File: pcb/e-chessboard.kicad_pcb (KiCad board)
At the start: 4 copper layers, 170 x 170 mm, 66 parts, among them J1 POWER, J2 UART, Q1 BC847, Q2 BC847, SW1 Reset, SW2 Boot, U1 ESP32-WROOM-32U, U10 MAGNET_LDR, U11 MAGNET_LDR, U12 MAGNET_LDR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

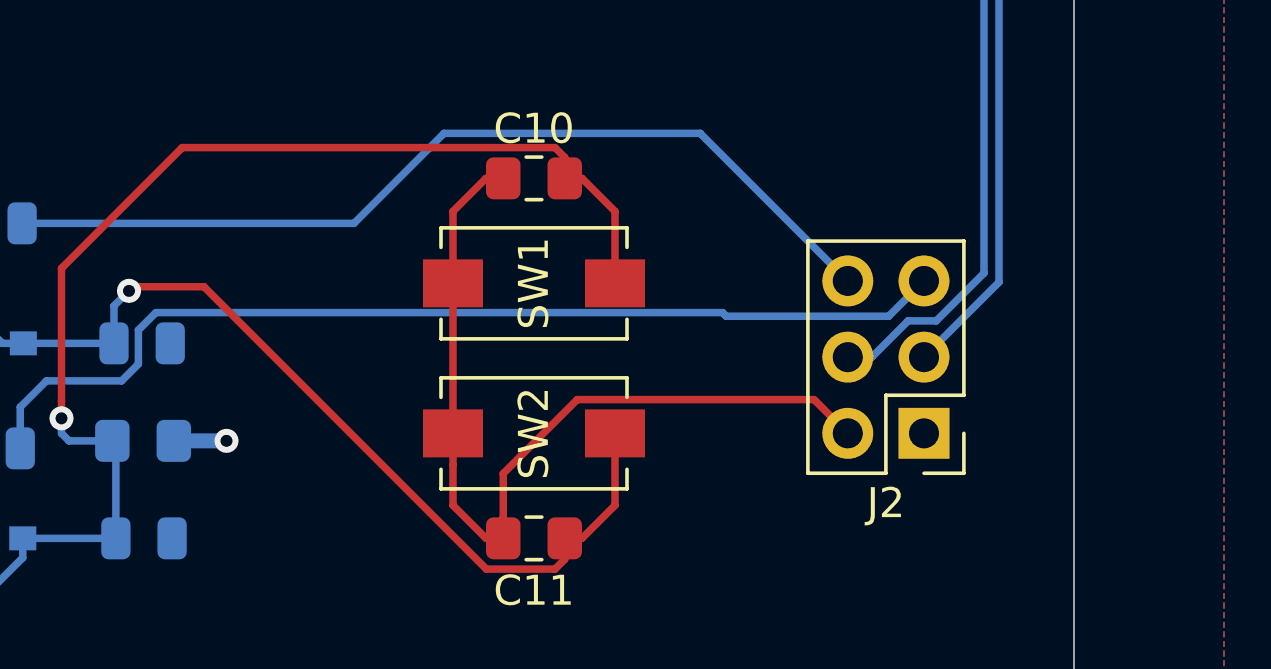
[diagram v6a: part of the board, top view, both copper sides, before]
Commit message: fix(kicad): adding label for taster and uart
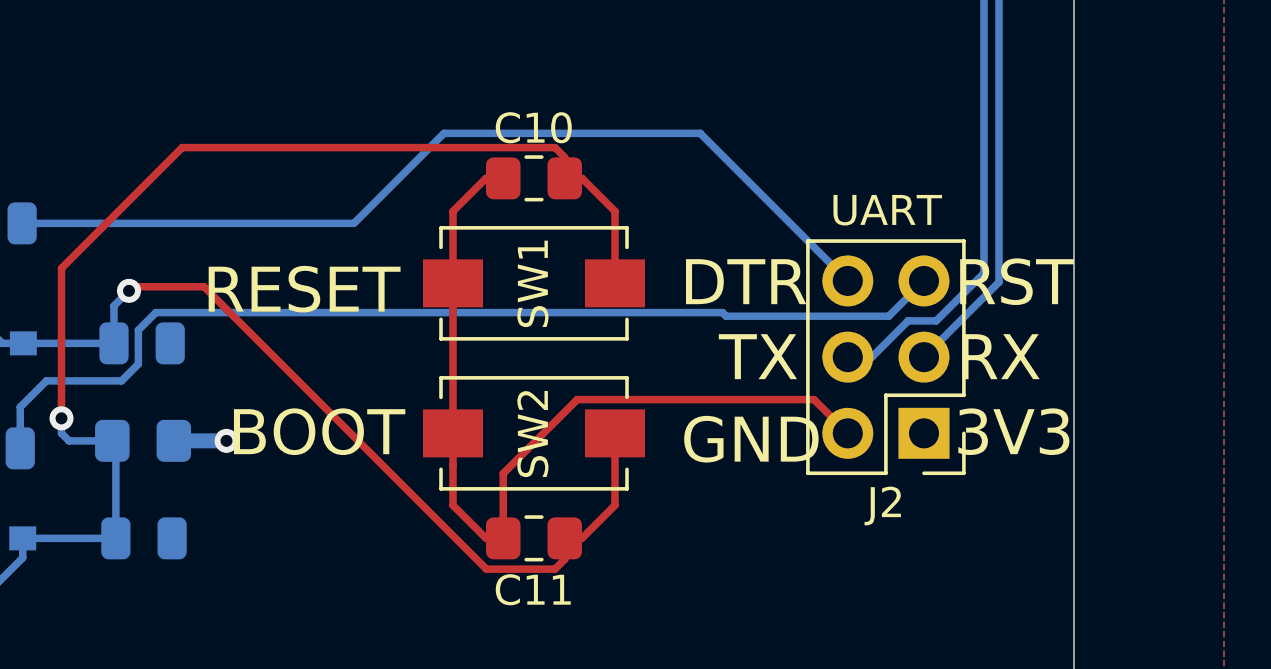
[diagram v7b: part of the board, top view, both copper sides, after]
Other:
- board text added: "3V3"
- board text added: "BOOT"
- board text added: "DTR"
- board text added: "GND"
- board text added: "RESET"
- board text added: "RST"
- board text added: "RX"
- board text added: "TX"
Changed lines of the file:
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@@
   (general
     (thickness 1.6)
-    (drawings 22)
+    (drawings 30)
     (tracks 537)
     (zones 0)
@@
       (effects (font (size 1 1) (thickness 0.15)))
     )
-    (fp_text value UART (at 1.27 7.41 180) (layer F.Fab)
+    (fp_text value UART (at 1.27 7.41 180) (layer F.SilkS)
       (effects (font (size 1 1) (thickness 0.15)))
     )
@@
     )
   )
+  (gr_text BOOT (at 194.75 112) (layer F.SilkS)
+    (effects (font (size 1.5 1.5) (thickness 0.3)))
+  )
+  (gr_text RESET (at 194.25 107.25) (layer F.SilkS)
+    (effects (font (size 1.5 1.5) (thickness 0.3)))
+  )
+  (gr_text DTR (at 209 107) (layer F.SilkS)
+    (effects (font (size 1.5 1.5) (thickness 0.3)))
+  )
+  (gr_text TX (at 209.5 109.5) (layer F.SilkS)
+    (effects (font (size 1.5 1.5) (thickness 0.3)))
+  )
+  (gr_text GND (at 209.25 112.25) (layer F.SilkS)
+    (effects (font (size 1.5 1.5) (thickness 0.3)))
+  )
+  (gr_text 3V3 (at 218 112) (layer F.SilkS)
+    (effects (font (size 1.5 1.5) (thickness 0.3)))
+  )
+  (gr_text RX (at 217.5 109.5) (layer F.SilkS)
+    (effects (font (size 1.5 1.5) (thickness 0.3)))
+  )
+  (gr_text RST (at 218 107) (layer F.SilkS)
+    (effects (font (size 1.5 1.5) (thickness 0.3)))
+  )
   (gr_line (start 220 55) (end 220 85) (layer Edge.Cuts) (width 0.05))
   (gr_line (start 220 215) (end 220 85) (layer Edge.Cuts) (width 0.05))
@@
     (connect_pads (clearance 0.508))
     (min_thickness 0.254)
-    (fill yes (arc_segments 32) (thermal_gap 0.508) (thermal_bridge_width 0.508))
+    (fill (arc_segments 32) (thermal_gap 0.508) (thermal_bridge_width 0.508))
     (polygon
       (pts
@@
     (connect_pads (clearance 0.508))
     (min_thickness 0.254)
-    (fill yes (arc_segments 32) (thermal_gap 0.508) (thermal_bridge_width 0.508))
+    (fill (arc_segments 32) (thermal_gap 0.508) (thermal_bridge_width 0.508))
     (polygon
       (pts
@@
     (connect_pads (clearance 0.508))
     (min_thickness 0.254)
-    (fill yes (arc_segments 32) (thermal_gap 0.508) (thermal_bridge_width 0.508))
+    (fill (arc_segments 32) (thermal_gap 0.508) (thermal_bridge_width 0.508))
     (polygon
       (pts
@@
     (connect_pads (clearance 0.508))
     (min_thickness 0.254)
-    (fill yes (arc_segments 32) (thermal_gap 0.508) (thermal_bridge_width 0.508))
+    (fill (arc_segments 32) (thermal_gap 0.508) (thermal_bridge_width 0.508))
     (polygon
       (pts

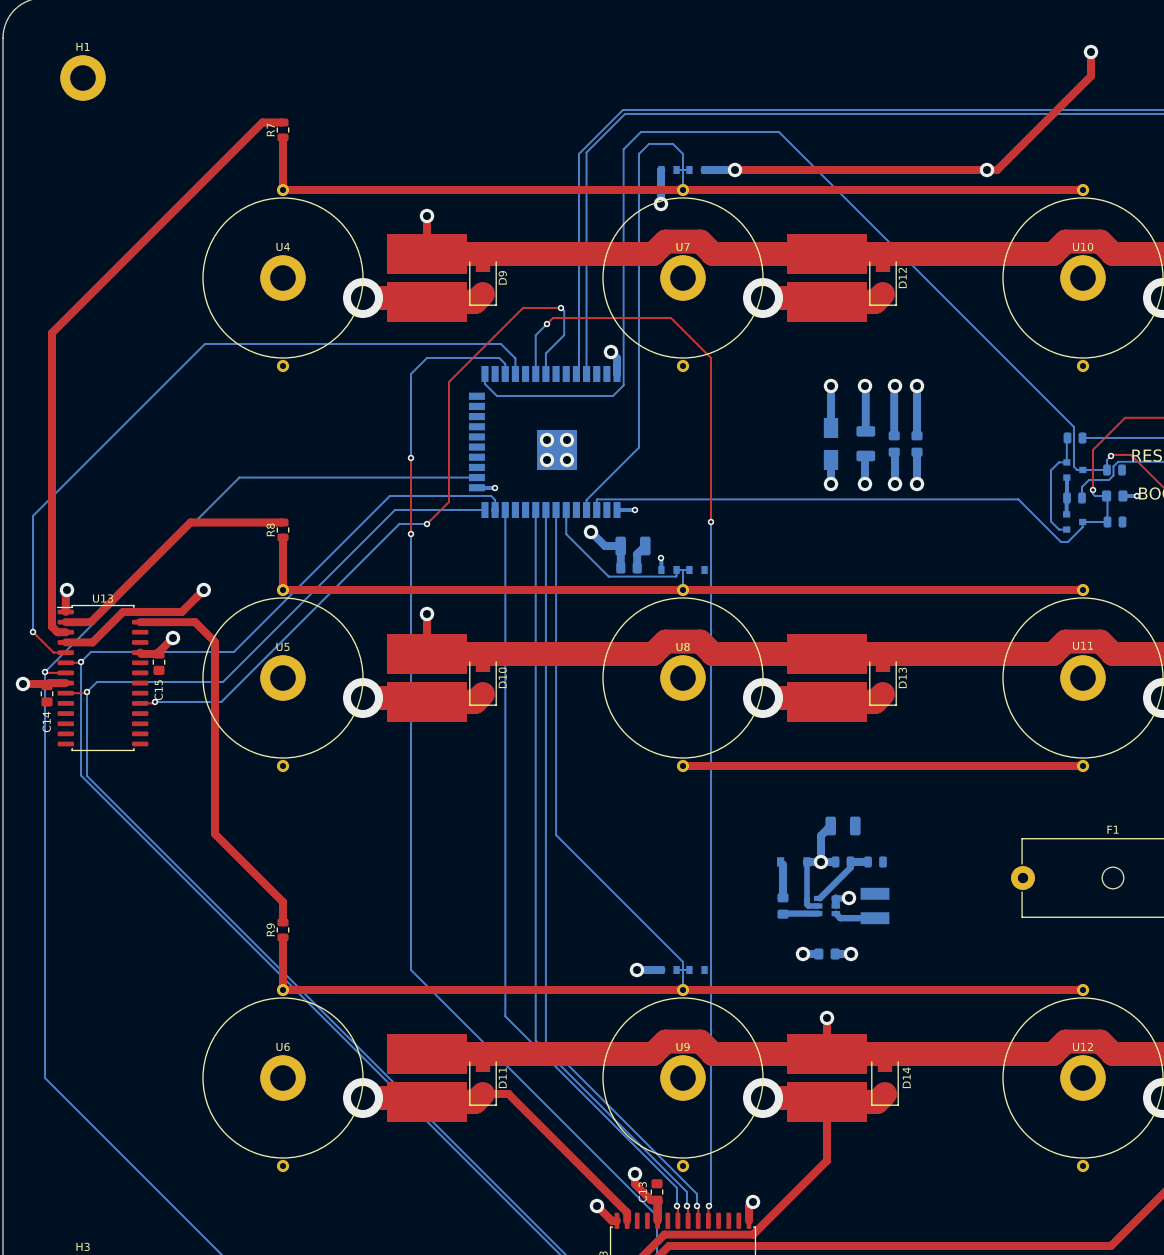
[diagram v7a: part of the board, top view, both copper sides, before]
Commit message: fix(kicad): redesign pcb
Redesigning the pcb with the new ldr matrix.
I'm pretty sure, that's it's still not working, but for the first
prototype I will put the focus on the magnets and not the ldr. Just a
prove a concept.
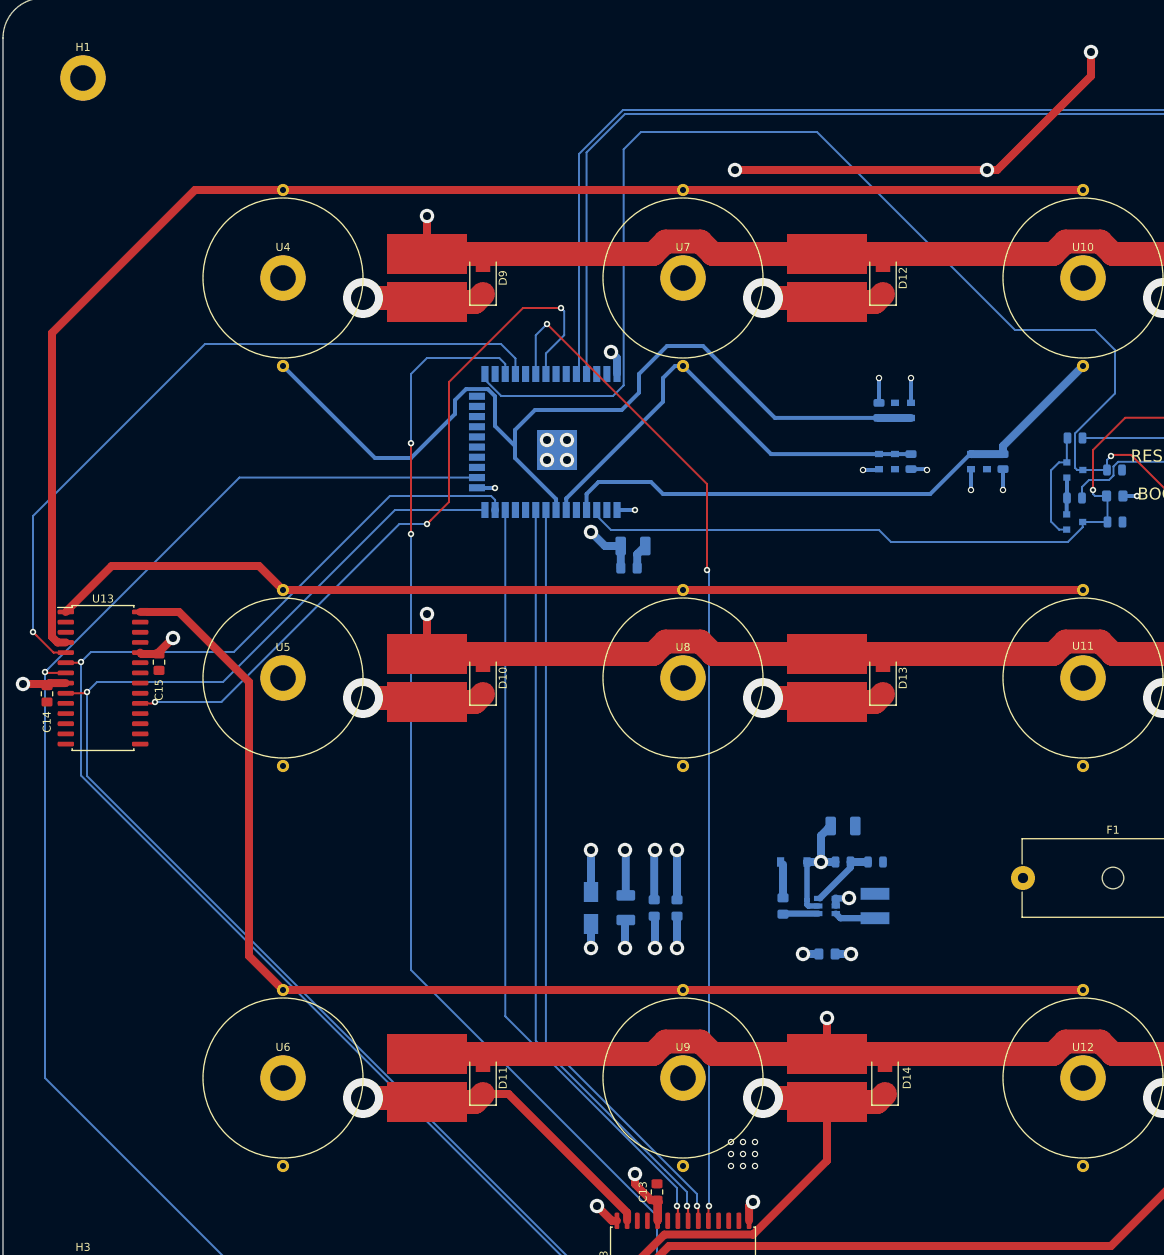
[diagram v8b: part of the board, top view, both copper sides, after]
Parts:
- R7, R8, R9: moved to B.Cu
- moved R9 107.4 mm to (175.0, 108.0), turned to 90 degrees
- moved R7 82.3 mm to (159.5, 101.5)
- moved R8 79.0 mm to (163.5, 108.0), turned to 90 degrees
- moved D5 76.2 mm to (163.5, 101.5), turned to 90 degrees
- moved D4 74.2 mm to (161.5, 101.5), turned to 270 degrees
- moved C1 65.3 mm to (127.8, 163.7)
- moved C2 65.3 mm to (131.4, 163.8)
- moved C5 65.3 mm to (134.2, 163.8)
- moved D3 65.3 mm to (123.5, 163.8)
- moved D2 52.5 mm to (171.0, 108.0), turned to 270 degrees
- moved D1 51.4 mm to (173.0, 108.0), turned to 90 degrees
- moved D7 29.5 mm to (159.5, 108.0), turned to 270 degrees
- moved D6 28.2 mm to (161.5, 108.0), turned to 90 degrees
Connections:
- D1 pad 2: LDR_ADC1 -> LDR_ADC3
- D2 pad 1: LDR_ADC1 -> LDR_ADC3
- D4 pad 2: LDR_ADC3 -> LDR_ADC1
- D5 pad 1: LDR_ADC3 -> LDR_ADC1
- R7 pad 1: LDR_ROW1 -> +12V
- R8 pad 1: LDR_ROW2 -> +12V
- R9 pad 1: LDR_ROW3 -> +12V
- U1 pad 4: LDR_ADC1 -> LDR_ADC3
- U1 pad 7: LDR_ADC3 -> LDR_ADC1
- U10 pad 3: LDR_ADC1 -> LDR_ROW1
- U10 pad 4: GND -> LDR_ADC3
- U11 pad 3: LDR_ADC2 -> LDR_ROW2
- U11 pad 4: GND -> LDR_ADC3
- U12 pad 3: LDR_ADC3 -> LDR_ROW3
- U12 pad 4: GND -> LDR_ADC3
- U13 pad 1: +12V -> LDR_ROW2
- U13 pad 2: LDR_ROW2 -> GND
- U13 pad 27: LDR_ROW3 -> GND
- U13 pad 28: +12V -> LDR_ROW3
- U13 pad 3: LDR_ROW1 -> GND
- U13 pad 4: +12V -> LDR_ROW1
- U4 pad 3: LDR_ADC1 -> LDR_ROW1
- U4 pad 4: GND -> LDR_ADC1
- U5 pad 3: LDR_ADC2 -> LDR_ROW2
- U5 pad 4: GND -> LDR_ADC1
- U6 pad 3: LDR_ADC3 -> LDR_ROW3
- U6 pad 4: GND -> LDR_ADC1
- U7 pad 3: LDR_ADC1 -> LDR_ROW1
- U7 pad 4: GND -> LDR_ADC2
- U8 pad 3: LDR_ADC2 -> LDR_ROW2
- U8 pad 4: GND -> LDR_ADC2
- U9 pad 3: LDR_ADC3 -> LDR_ROW3
- U9 pad 4: GND -> LDR_ADC2
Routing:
- net LDR_ROW3: track 49.0 -> 157.5 mm
- net LDR_ROW2: track 32.3 -> 130.8 mm
- net LDR_ROW1: track 78.5 -> 176.3 mm
- net LDR_ADC1: track 168.0 -> 220.6 mm
- net GND: track 138.4 -> 87.3 mm, vias 18 -> 27
- net LDR_ADC2: track 130.5 -> 165.5 mm
- net +12V: track 80.9 -> 65.9 mm, vias 12 -> 13
- net IO0: track 156.8 -> 169.3 mm
- net MAG_EN: track 137.7 -> 127.4 mm
- net LDR_ADC3: track 174.7 -> 180.6 mm
- net +3V3: track 70.4 -> 66.6 mm
- net EN: track 103.2 -> 101.7 mm
